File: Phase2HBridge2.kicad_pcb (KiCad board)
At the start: 2 copper layers, 127 x 101.6 mm, 40 parts, among them J1 CONN-01X06-TerminalBlock-3.5m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, J2 CONN-FASTON-0.250, J4 CONN-FASTON-0.250, Q1 FET-NCH-400V-26A-TO220-FDP26N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, Q2 FET-NCH-400V-26A-TO220-FDP26N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, Q3 FET-NCH-400V-26A-TO220-FDP26N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, Q4 FET-NCH-400V-26A-TO220-FDP26N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, U1 IC-Driver-HalfBridge-FAN7393A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, U2 IC-Driver-HalfBridge-FAN7393A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

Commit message: Parts Placed - Need to Route
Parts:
- moved R6 154.7 mm to (129.0, 88.7)
- moved C5 154.2 mm to (42.6, 97.6)
- moved R5 153.5 mm to (42.6, 91.2), turned to 180 degrees
- moved R8 152.9 mm to (42.6, 93.8)
- moved C8 145.4 mm to (129.0, 82.4)
- moved R9 138.2 mm to (129.0, 84.9)
- moved R7 117.9 mm to (55.1, 68.2), turned to 90 degrees
- moved H4 50.6 mm to (121.5, 121.5)
- moved H3 47.4 mm to (121.5, 50.0)
- moved D10 45.3 mm to (122.6, 93.8)
- moved U2 45.3 mm to (122.6, 86.2)
- moved C7 37.6 mm to (115.0, 90.0)
- moved Q4 35.1 mm to (104.8, 100.1)
- moved R4 35.1 mm to (109.9, 102.7), turned to 180 degrees
- moved D8 35.0 mm to (109.9, 98.9), turned to 90 degrees
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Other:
- board size 127 x 101.6 mm -> 97.5 x 97.5 mm

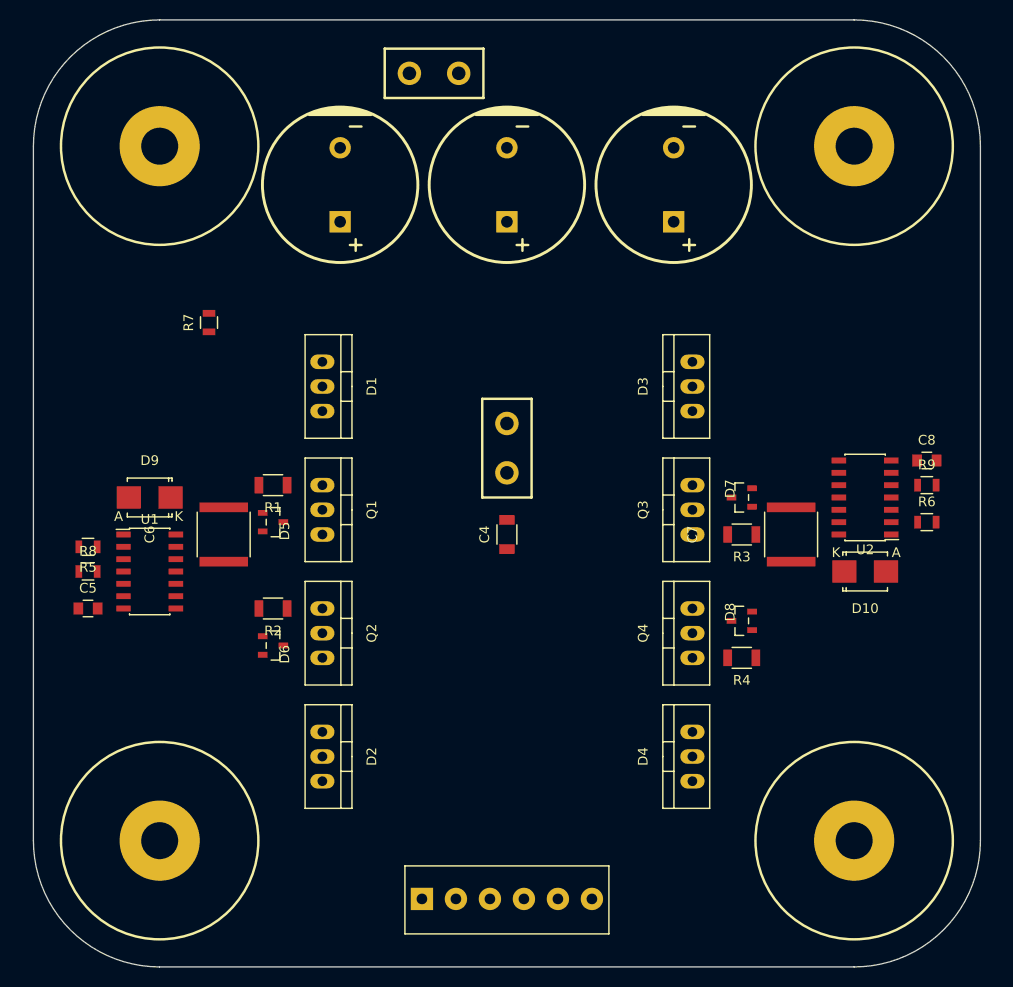
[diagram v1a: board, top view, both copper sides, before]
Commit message: Finished Layout
Need to Verify Layout, add graphics, update refused locations, etc…
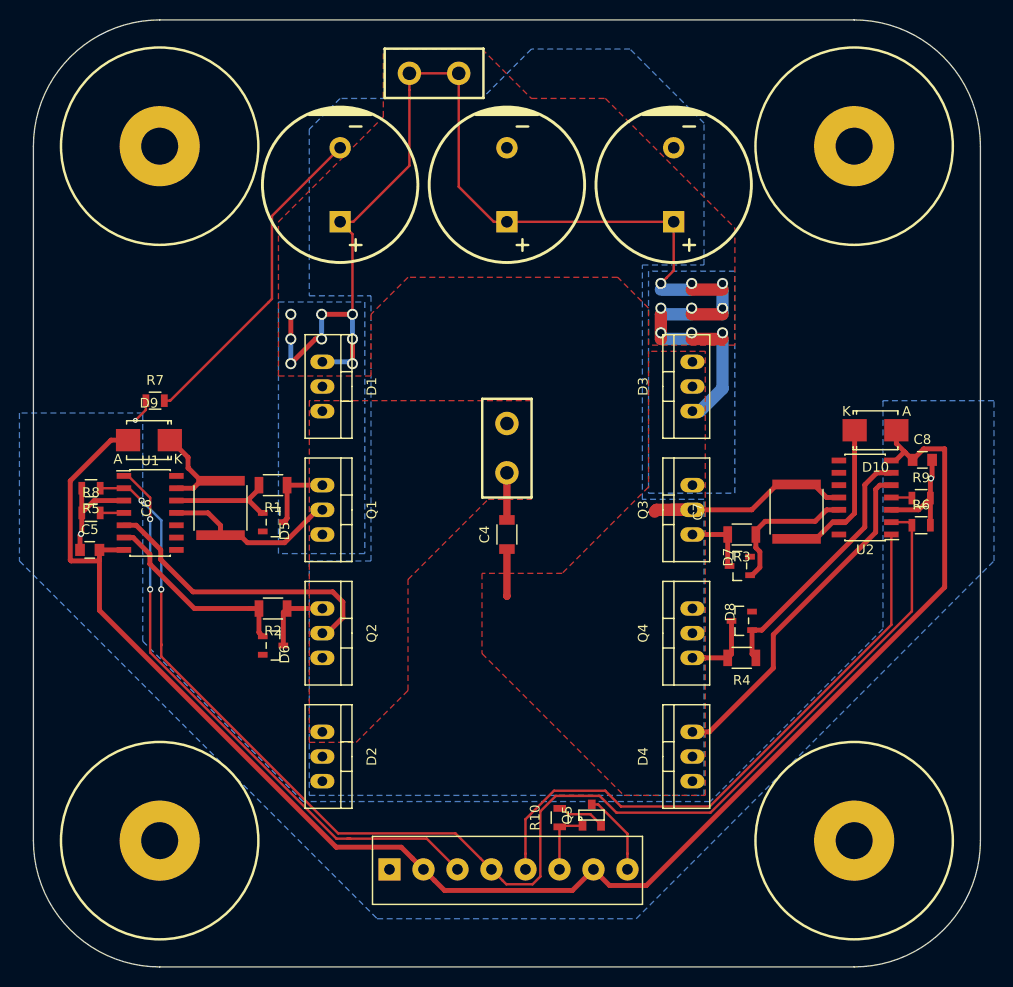
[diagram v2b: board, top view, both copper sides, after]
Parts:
- added Q5: BSS138, SOT-23, F.Cu at (94.5, 118.9)
- added R10: RES-10k-.125W-1%-0805-ERJ-6ENF1002V, Resistors_SMD:R_0805, F.Cu at (91.2, 119.1)
- J1: value CONN-01X06-TerminalBlock-3.5mm-Side-1776275-6 -> CONN-01X08-TerminalBlock-3.5mm-Side-1776275-8; footprint Phase2HBridge2:CON-TerminalBlock-6Pos-Side-3.5MM-1776275-6 -> Phase2HBridge2:CON-TerminalBlock-8Pos-Side-3.5MM-1776275-8
- moved D10 14.6 mm to (123.7, 79.2)
- moved R7 9.77 mm to (49.5, 76.2), turned to 0 degrees
- moved D7 7.05 mm to (109.7, 93.2)
- moved R5 6.04 mm to (42.9, 85.2)
- moved R8 6.04 mm to (42.9, 87.8)
- moved C5 6.04 mm to (42.8, 91.6)
- moved U1 6.03 mm to (49.0, 87.8)
- moved D9 5.91 mm to (48.9, 80.3)
- moved J1 4.52 mm to (73.7, 124.5)
- moved C6 2.75 mm to (56.3, 87.2)
- moved C7 2.42 mm to (115.6, 87.6)
- moved R9 1.45 mm to (128.4, 86.2)
- moved R6 0.66 mm to (128.4, 89.0)
- moved C8 0.46 mm to (128.5, 82.3)
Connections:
- J1 pad 3: ENABLE -> PWM_M+
- J1 pad 4: PWM_M- -> ENABLE
- J1 pad 5: PWM_M+ -> PWM_M-
- J1 pad 6: VSS -> PWM_FAN
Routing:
- net VDD: track 0.00 -> 164.5 mm
- net ENABLE: track 0.00 -> 136.8 mm, vias 0 -> 2
- net VPP: track 0.00 -> 132.9 mm, vias 0 -> 17
- net GND: track 0.00 -> 100.8 mm
- net PWM_M-: track 0.00 -> 61.8 mm
- net PWM_M+: track 0.00 -> 60.7 mm, vias 0 -> 2
- net VSS: track 0.00 -> 30.2 mm, vias 0 -> 3
- net /MOTOR-: track 0.00 -> 27.7 mm
- net /LO_M-: track 0.00 -> 26.6 mm
- net /MOTOR+: track 0.00 -> 23.1 mm
- net /LO_M+: track 0.00 -> 20.5 mm
- net /Vb_M-: track 0.00 -> 15.6 mm
- net /HO_M-: track 0.00 -> 14.7 mm
- net /Vb_M+: track 0.00 -> 12.5 mm
- net /HO_M+: track 0.00 -> 11.7 mm
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- added copper zone on F.Cu, net /MOTOR+
- added copper zone on F.Cu, net /MOTOR-
- added copper zone on B.Cu, net GND
- added copper zone on B.Cu, net VPP
- added copper zone on F.Cu, net VPP
- added copper zone on B.Cu, net VSS
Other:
- net class 12V added: clearance 0.254, trace_width 0.508, via_dia 0.635, via_drill 0.381
- net class 90V added: clearance 0.6096, trace_width 0.762, via_dia 1.143, via_drill 0.762
- net class Default: via_dia 0.889 -> 0.635; via_drill 0.635 -> 0.381
- rule trace_min: 0.254 -> 0.2032
- rule via_min_drill: 0.508 -> 0.254
- rule via_min_size: 0.889 -> 0.508
